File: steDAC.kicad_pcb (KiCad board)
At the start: 2 copper layers, 100 x 80 mm, 152 parts, among them IC10 TPS7A3001DGNT, IC11 ADP150AUJZ-3.3-R7, IC2 ES9038Q2M, IC3 ATSAMS70N20A-AN, IC4 ADP150AUJZ-3.3-R7, IC5 ADP150AUJZ-3.3-R7, IC6 ADP150AUJZ-3.3-R7, IC7 ADP150AUJZ-3.3-R7, IC8 LT1026CS8#PBF, IC9 ADP7118ARDZ, J2 USB4105-GF-A, J3 Conn_02x05_Odd_Even, J5 Conn_01x02, J6 Conn_01x04, J7 STX-3120-5B-284C, U2 OPA1612-Q1, U3 OPA1612-Q1, U4 OPA1622, Y2 SiT8209AI-21-33S-100.000000X, Y3 12MHz

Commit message: Updating stuff
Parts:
- C45, C46, C47: value 47u_16V -> 47u
- C72: value 0.1uF -> 0.1u
- R23, R24, R26, R27: value 350 -> 352
- R31: value 23k -> 24k

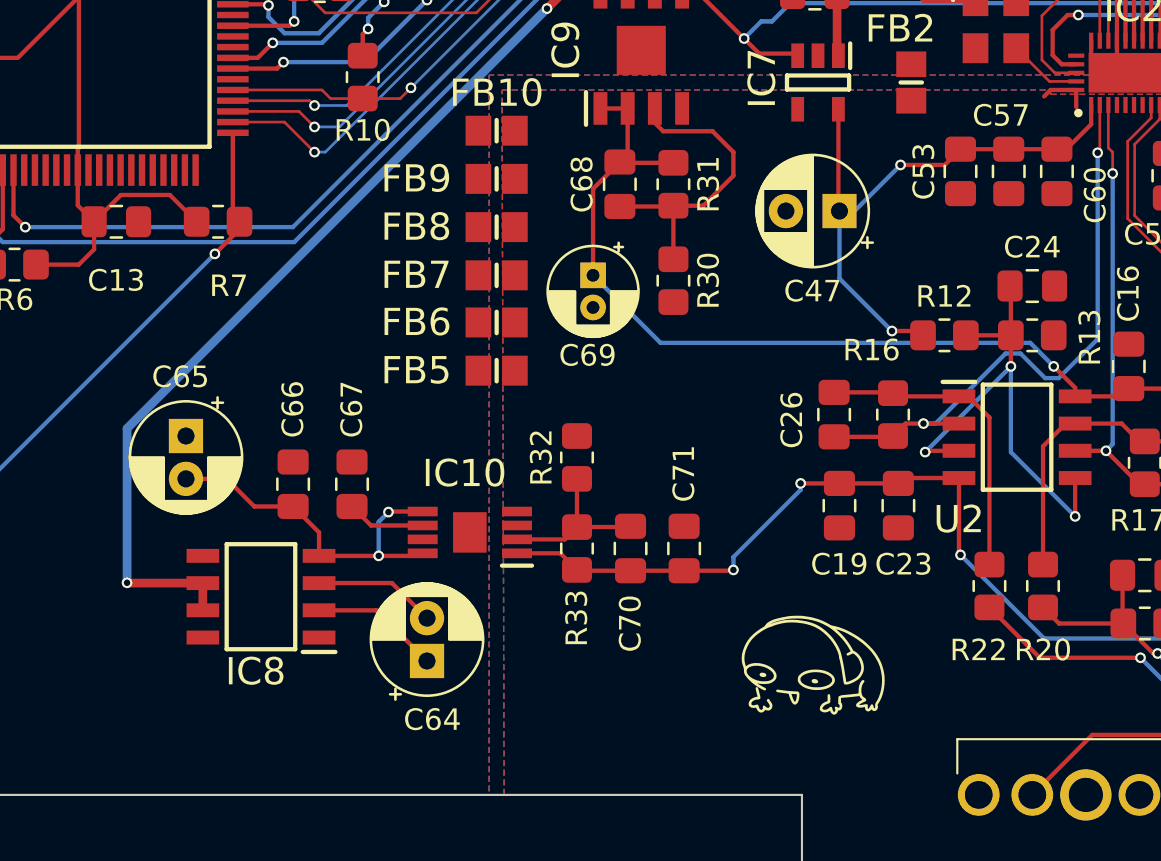
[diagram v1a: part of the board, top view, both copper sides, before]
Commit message: Changing negative rail power supply
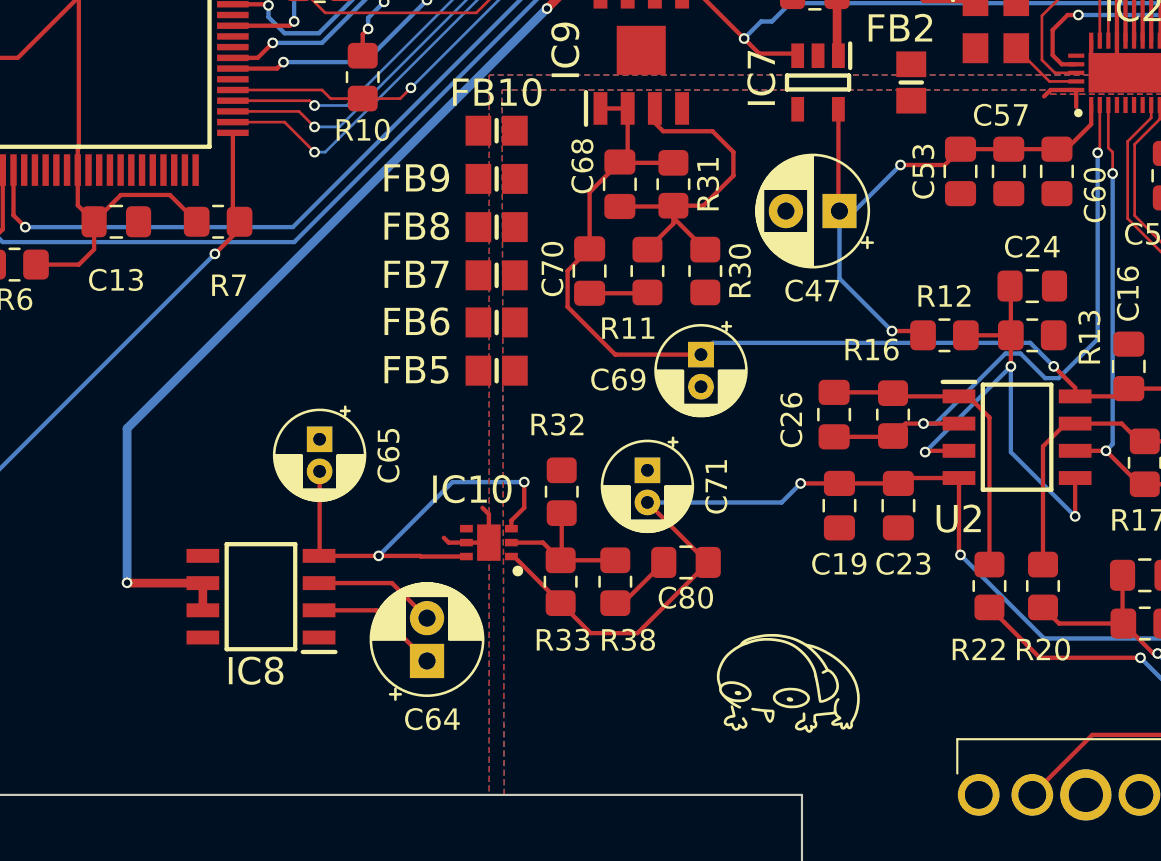
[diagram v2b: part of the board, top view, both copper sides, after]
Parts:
- removed C66: 10u, Capacitor_SMD:C_0805_2012Metric_Pad1.18x1.45mm_HandSolder
- removed C67: 10n, Capacitor_SMD:C_0805_2012Metric_Pad1.18x1.45mm_HandSolder
- added C80: 1u, Capacitor_SMD:C_0805_2012Metric_Pad1.18x1.45mm_HandSolder, F.Cu at (137.5, 115.8)
- added R11: 1k, Resistor_SMD:R_0805_2012Metric_Pad1.20x1.40mm_HandSolder, F.Cu at (135.7, 102.2)
- added R38: 10k, Resistor_SMD:R_0805_2012Metric_Pad1.20x1.40mm_HandSolder, F.Cu at (134.2, 116.7)
- C65: value 1u -> 2.2u; footprint Capacitor_THT:CP_Radial_D5.0mm_P2.00mm -> Capacitor_THT:CP_Radial_D4.0mm_P1.50mm
- C70: value 10n -> 10u
- C71: value 10u -> 2.2u; footprint Capacitor_SMD:C_0805_2012Metric_Pad1.18x1.45mm_HandSolder -> Capacitor_THT:CP_Radial_D4.0mm_P1.50mm
- IC10: value TPS7A3001DGNT -> ADP7182ACPZN-R7; footprint SamacSys_Parts:SOP65P490X110-9N -> SamacSys_Parts:SON65P200X200X65-7N-D
- R5: value 5.6k -> 5.62k
- moved C70 13.1 mm to (133.0, 102.2), turned to 90 degrees
- moved C69 6.25 mm to (138.2, 106.1)
- moved C65 6.24 mm to (120.4, 110.0)
- moved C71 4.03 mm to (135.7, 111.5), turned to -90 degrees
- moved R32 1.75 mm to (131.7, 112.5), turned to -90 degrees
- moved R33 1.73 mm to (131.7, 116.7), turned to -90 degrees
- moved R30 1.55 mm to (138.4, 102.2)
- moved G*** 1.44 mm to (142.6, 121.5)
- moved IC10 1.01 mm to (128.3, 114.9)
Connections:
- C65 pad 2: Net-(C65-Pad2) -> Net-(IC8-Pad4)
- C70 pad 2: -VDAC -> +VDAC
- C71 pad 1: -VDAC -> GNDREF
- C71 pad 2: GNDREF -> -VDAC
- IC10 pad 2: Net-(C70-Pad1) -> Net-(R32-Pad2)
- IC10 pad 3: unconnected-(IC10-Pad3) -> Net-(IC8-Pad4)
- IC10 pad 4: GNDREF -> unconnected-(IC10-Pad4)
- IC10 pad 5: Net-(C65-Pad2) -> GND
- IC10 pad 6: Net-(C67-Pad1) -> Net-(IC8-Pad4)
- IC10 pad 7: unconnected-(IC10-Pad7) -> GND
- IC8 pad 4: Net-(C65-Pad2) -> Net-(IC8-Pad4)
- R32 pad 1: Net-(C70-Pad1) -> GNDREF
- R32 pad 2: GNDREF -> Net-(R32-Pad2)
- R33 pad 1: -VDAC -> Net-(R32-Pad2)
- R33 pad 2: Net-(C70-Pad1) -> -VDAC
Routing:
- net Net-(IC8-Pad4): track 0.00 -> 21.5 mm, vias 0 -> 2
- net Net-(C65-Pad2): track 17.1 -> 0.00 mm, vias 2 -> 0
- net -VDAC: track 85.5 -> 93.3 mm, vias 5 -> 4
- net Net-(R32-Pad2): track 0.00 -> 7.41 mm
- net Net-(C70-Pad1): track 7.80 -> 2.72 mm
- net GND: track 24.0 -> 28.0 mm
- net Net-(C67-Pad1): track 3.67 -> 0.00 mm
- net Net-(C80-Pad2): track 0.00 -> 3.05 mm
- net +VDAC: track 84.9 -> 87.9 mm
- net Net-(C68-Pad1): track 14.4 -> 17.1 mm

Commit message: Trace edits
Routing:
- net GND: track 28.0 -> 30.7 mm

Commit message: updates
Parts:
- added C66: 4.7u, Capacitor_SMD:C_0805_2012Metric_Pad1.18x1.45mm_HandSolder, F.Cu at (112.5, 117.8)
- moved C65 0.74 mm to (120.7, 110.8)
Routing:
- net DAC_5V: track 134.4 -> 138.3 mm
- net Net-(C65-Pad2): track 21.5 -> 19.1 mm
